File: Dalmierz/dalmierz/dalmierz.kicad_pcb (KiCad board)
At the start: 2 copper layers, 4.3 x 6.2 mm, 51 parts, among them IC1 W25Q16JVUXIQ, J1 690-005-298-486, J2 B4B-ZR_LF__SN_TF LUNA, J3 B4B-ZR_LF__SN_LCD I2C, J7 B4B-ZR_LF__SN_URM13, SW1 1-1825910-4, SW2 1-1825910-4, SW3 1-1825910-4, SW4 1-1825910-4, SW5 1-1825910-4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

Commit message: MAIN: footprinty, rozmieszczenie na PCB work in progress
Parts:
- C1, C12, C13, C14, C18, C2, C21, C22: footprint Capacitor_SMD:C_0805_2012Metric -> Capacitor_SMD:C_0603_1608Metric
- C16, C17: footprint Capacitor_SMD:C_1210_3225Metric -> Capacitor_SMD:C_0603_1608Metric
- C19, C20: footprint Capacitor_SMD:C_1206_3216Metric -> Capacitor_SMD:C_0603_1608Metric
- J2: value B4B-ZR_LF__SN_TF LUNA -> B4B-ZR TF LUNA
- J3: value B4B-ZR_LF__SN_LCD I2C -> B4B-ZR LCD
- J7: value B4B-ZR_LF__SN_URM13 -> B4B-ZR URM13
- R11: renamed from R1; footprint Resistor_SMD:R_1210_3225Metric -> Resistor_SMD:R_0603_1608Metric
- R12, R13, R14, R2, R3: footprint Resistor_SMD:R_1210_3225Metric -> Resistor_SMD:R_0603_1608Metric
- R7: footprint Resistor_SMD:R_0805_2012Metric -> Resistor_SMD:R_0603_1608Metric
- R9: footprint Resistor_SMD:R_1206_3216Metric -> Resistor_SMD:R_0603_1608Metric
- moved BT1 92.1 mm to (160.0, 108.0), turned to -90 degrees
- moved R14 89.7 mm to (140.2, 137.4)
- moved B1 84.1 mm to (118.0, 146.5), turned to 0 degrees
- moved IC1 72.3 mm to (115.7, 109.3)
- moved C19 67.7 mm to (140.9, 84.9)
- moved U5 64.6 mm to (145.2, 86.0)
- moved C12 64.5 mm to (136.1, 114.4)
- moved R9 64.2 mm to (145.2, 109.4)
- moved C14 63.7 mm to (145.2, 114.4)
- moved C13 63.5 mm to (140.2, 114.4)
- moved C7 63.1 mm to (142.2, 121.4)
- moved R12 62.9 mm to (130.2, 108.4)
- moved R13 62.9 mm to (135.2, 108.4)
- moved J2 62.3 mm to (105.5, 124.1)
- moved J3 62.3 mm to (105.5, 129.1)
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- renumbered SW7_BOOTSEL1 to SW
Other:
- outline, holes or cut-outs redrawn

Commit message: MAIN: PCB traces in progress.
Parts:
- J2: value B4B-ZR TF LUNA -> B4B-ZR_LF__SN_TF LUNA
- J3: value B4B-ZR LCD -> B4B-ZR_LF__SN_LCD I2C
- J7: value B4B-ZR URM13 -> B4B-ZR_LF__SN_URM13
- moved J7 38.8 mm to (122.9, 99.2), turned to 180 degrees
- moved C16 34.6 mm to (131.3, 108.4), turned to 180 degrees
- moved C19 34.0 mm to (131.5, 117.6)
- moved C17 33.6 mm to (135.2, 109.4), turned to 180 degrees
- moved SW7 33.0 mm to (123.8, 90.9), turned to 0 degrees
- moved D3 32.9 mm to (122.2, 116.9), turned to 0 degrees
- moved C1 32.2 mm to (146.1, 115.7)
- moved U5 31.1 mm to (131.8, 114.1), turned to 90 degrees
- moved Y1 31.0 mm to (134.8, 107.4)
- moved J3 30.9 mm to (122.9, 103.5), turned to 180 degrees
- moved R14 30.8 mm to (137.9, 106.7), turned to -90 degrees
- moved R2 29.7 mm to (129.2, 113.1), turned to -90 degrees
- moved C2 29.3 mm to (145.2, 110.9), turned to 0 degrees
- moved U4 28.5 mm to (124.1, 114.2)
- moved U2 27.7 mm to (144.4, 113.3), turned to 0 degrees
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- renumbered SW to SW7
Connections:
- R2 pad 1: Net-(U5-SCL) -> /SCL0
- R3 pad 2: Net-(U5-SDA) -> /SDA0
- U5 pad 7: Net-(U5-SDA) -> /SDA0
- U5 pad 8: Net-(U5-SCL) -> /SCL0
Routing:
- net +3V3: track 0.00 -> 128.4 mm, vias 0 -> 5
- net /BTN6: track 0.00 -> 78.2 mm, vias 0 -> 1
- net /BTN3: track 0.00 -> 72.2 mm, vias 0 -> 1
- net VBUS: track 0.00 -> 70.4 mm, vias 0 -> 1
- net /BTN5: track 0.00 -> 67.5 mm, vias 0 -> 1
- net /BTN2: track 0.00 -> 60.8 mm, vias 0 -> 1
- net /BTN4: track 0.00 -> 59.1 mm, vias 0 -> 1
- net GND: track 0.00 -> 54.0 mm
- net /BTN1: track 0.00 -> 45.8 mm, vias 0 -> 1
- net /SDA0: track 0.00 -> 34.1 mm
- net /SCL0: track 0.00 -> 28.5 mm, vias 0 -> 2
- net +1V1: track 0.00 -> 25.8 mm, vias 0 -> 2
- net /QSPI_SD3: track 0.00 -> 11.9 mm
- net /QSPI_SCLK: track 0.00 -> 10.7 mm
- net /QSPI_SS: track 0.00 -> 10.2 mm
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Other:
- outline, holes or cut-outs redrawn

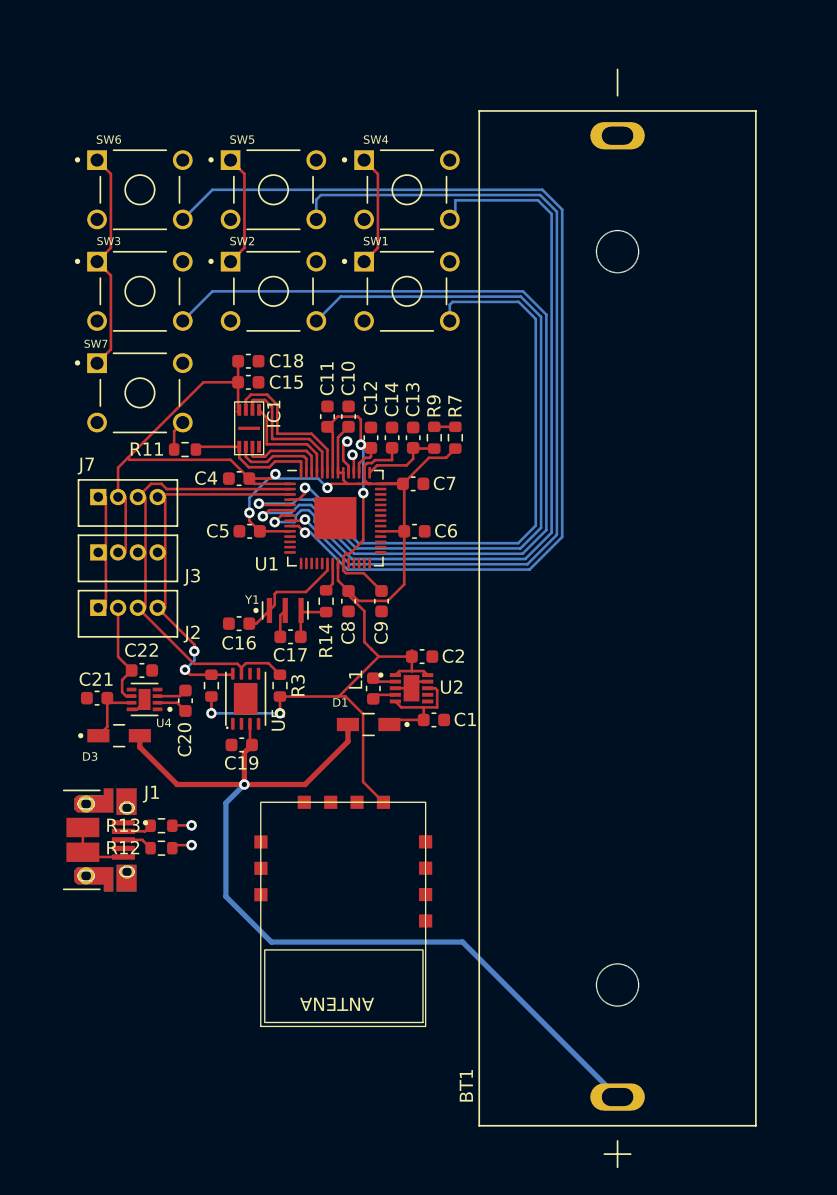
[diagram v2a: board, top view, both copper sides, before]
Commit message: MAIN: rozwiazanie problemow PCB
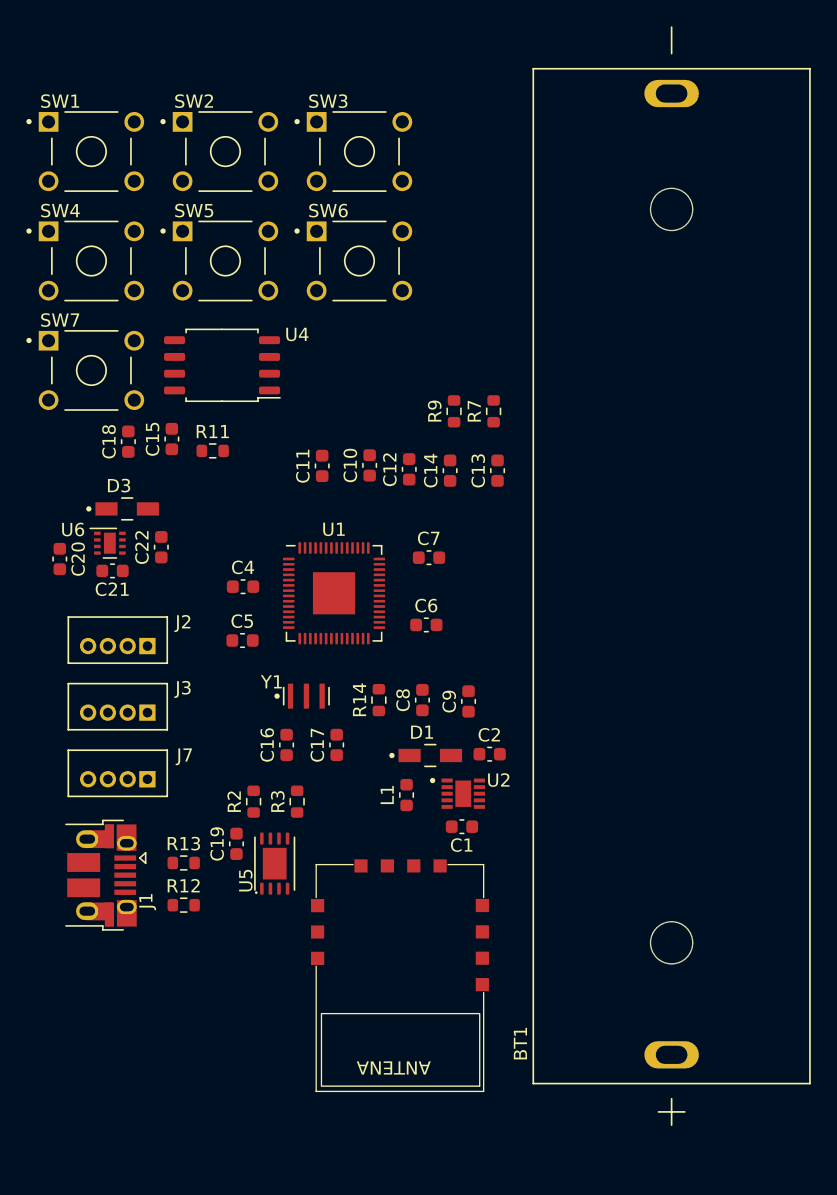
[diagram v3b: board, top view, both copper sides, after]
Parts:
- removed IC1: W25Q16JVUXIQ, W25Q16JVUXIQ:SON50P300X200X60-9N
- added U6: LM2775DSG, Package_SON:WSON-8-1EP_2x2mm_P0.5mm_EP0.9x1.6mm, F.Cu at (121.5, 102.3)
- J1: value 690-005-298-486 -> USB_B_Micro; footprint 690-005-298-486:EDAC_690-005-298-486 -> Connector_USB:USB_Micro-B_Amphenol_10103594-0001LF_Horizontal
- U4: value LM2775DSGT -> W25Q32JVSS; footprint LM2775DSGT:SON50P200X200X80-9N -> Package_SO:SOIC-8_5.23x5.23mm_P1.27mm
- moved SW1 26.2 mm to (120.1, 72.6)
- moved U4 26.0 mm to (130.0, 88.8)
- moved SW4 24.5 mm to (120.1, 80.9)
- moved J7 20.5 mm to (122.1, 119.8), turned to 0 degrees
- moved SW3 19.7 mm to (140.4, 72.6)
- moved SW6 17.5 mm to (140.4, 80.9)
- moved D3 17.2 mm to (122.8, 99.7)
- moved C20 14.4 mm to (117.7, 103.5)
- moved U5 12.7 mm to (134.0, 126.6)
- moved J3 11.3 mm to (122.1, 114.7), turned to 0 degrees
- moved SW2 11.2 mm to (130.3, 72.6)
- moved C18 11.0 mm to (122.9, 94.6), turned to 90 degrees
- moved C9 10.1 mm to (148.7, 114.3), turned to 90 degrees
- moved C16 9.88 mm to (134.9, 117.6), turned to 90 degrees
- moved C21 9.72 mm to (121.7, 104.4), turned to 180 degrees
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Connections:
- C20 pad 1: Net-(U4-C1+) -> Net-(U6-C1-)
- C20 pad 2: Net-(U4-C1-) -> Net-(U6-C1+)
- C21 pad 2: Net-(U4-VIN) -> Net-(U6-VIN)
- D3 pad 1: Net-(U4-VIN) -> Net-(U6-VIN)
- U4 pad 1: unconnected-(U4-PFM-Pad1) -> /QSPI_SS
- U4 pad 2: Net-(U4-C1-) -> /QSPI_SD1
- U4 pad 3: Net-(U4-C1+) -> /QSPI_SD2
- U4 pad 4: unconnected-(U4-OUTDIS-Pad4) -> GND
- U4 pad 5: unconnected-(U4-EN-Pad5) -> /QSPI_SD0
- U4 pad 6: +5V -> /QSPI_SCLK
- U4 pad 7: Net-(U4-VIN) -> /QSPI_SD3
- U4 pad 8: GND -> +3V3
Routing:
- net +3V3: track 128.4 -> 0.00 mm, vias 5 -> 0
- net /BTN6: track 78.2 -> 0.00 mm, vias 1 -> 0
- net /BTN3: track 72.2 -> 0.00 mm, vias 1 -> 0
- net VBUS: track 70.4 -> 0.00 mm, vias 1 -> 0
- net /BTN5: track 67.5 -> 0.00 mm, vias 1 -> 0
- net /BTN2: track 60.8 -> 0.00 mm, vias 1 -> 0
- net /BTN4: track 59.1 -> 0.00 mm, vias 1 -> 0
- net GND: track 54.0 -> 0.00 mm
- net /BTN1: track 45.8 -> 0.00 mm, vias 1 -> 0
- net /SDA0: track 34.1 -> 0.00 mm
- net /SCL0: track 28.5 -> 0.00 mm, vias 2 -> 0
- net +1V1: track 25.8 -> 0.00 mm, vias 2 -> 0
- net /QSPI_SD3: track 11.9 -> 0.00 mm
- net /QSPI_SCLK: track 10.7 -> 0.00 mm
- net /QSPI_SS: track 10.2 -> 0.00 mm
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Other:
- board outline removed

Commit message: MAIN: Koniec tworzenia PBC.
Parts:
- moved R12 36.0 mm to (131.7, 94.0)
- moved J1 34.9 mm to (127.0, 93.1)
- moved R13 34.5 mm to (131.7, 92.4)
- moved SW7 28.3 mm to (148.2, 85.2)
- moved SW4 28.3 mm to (148.2, 77.2)
- moved SW1 28.3 mm to (148.2, 69.3)
- moved C18 20.6 mm to (141.2, 85.2)
- moved R11 16.9 mm to (142.8, 85.2), turned to -90 degrees
- moved C15 16.3 mm to (139.6, 85.2)
- moved C16 13.4 mm to (143.3, 107.1), turned to 0 degrees
- moved C19 12.6 mm to (139.2, 115.5), turned to 0 degrees
- moved SW6 11.6 mm to (129.4, 77.2)
- moved SW3 11.5 mm to (129.4, 69.3)
- moved C4 10.3 mm to (137.8, 97.4)
- moved C21 10.3 mm to (131.8, 102.8)
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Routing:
- net GND: track 0.00 -> 270.1 mm
- net +3V3: track 0.00 -> 141.8 mm, vias 0 -> 6
- net /BTN3: track 0.00 -> 85.8 mm, vias 0 -> 1
- net /BTN2: track 0.00 -> 79.5 mm, vias 0 -> 1
- net VBUS: track 0.00 -> 77.6 mm, vias 0 -> 3
- net /BTN1: track 0.00 -> 73.1 mm, vias 0 -> 1
- net /BTN6: track 0.00 -> 68.2 mm, vias 0 -> 1
- net /BT_INTERRUPT: track 0.00 -> 64.6 mm, vias 0 -> 2
- net /BTN5: track 0.00 -> 62.9 mm, vias 0 -> 1
- net /BT_POWER_DOWN: track 0.00 -> 59.4 mm, vias 0 -> 2
- net /BT_LOW_POWER: track 0.00 -> 57.4 mm, vias 0 -> 2
- net /BTN4: track 0.00 -> 57.1 mm, vias 0 -> 1
- net /UART0_RX: track 0.00 -> 50.2 mm, vias 0 -> 2
- net +1V1: track 0.00 -> 49.6 mm, vias 0 -> 5
- net /UART0_TX: track 0.00 -> 49.1 mm, vias 0 -> 2
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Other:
- board outline added: 54 x 87 mm

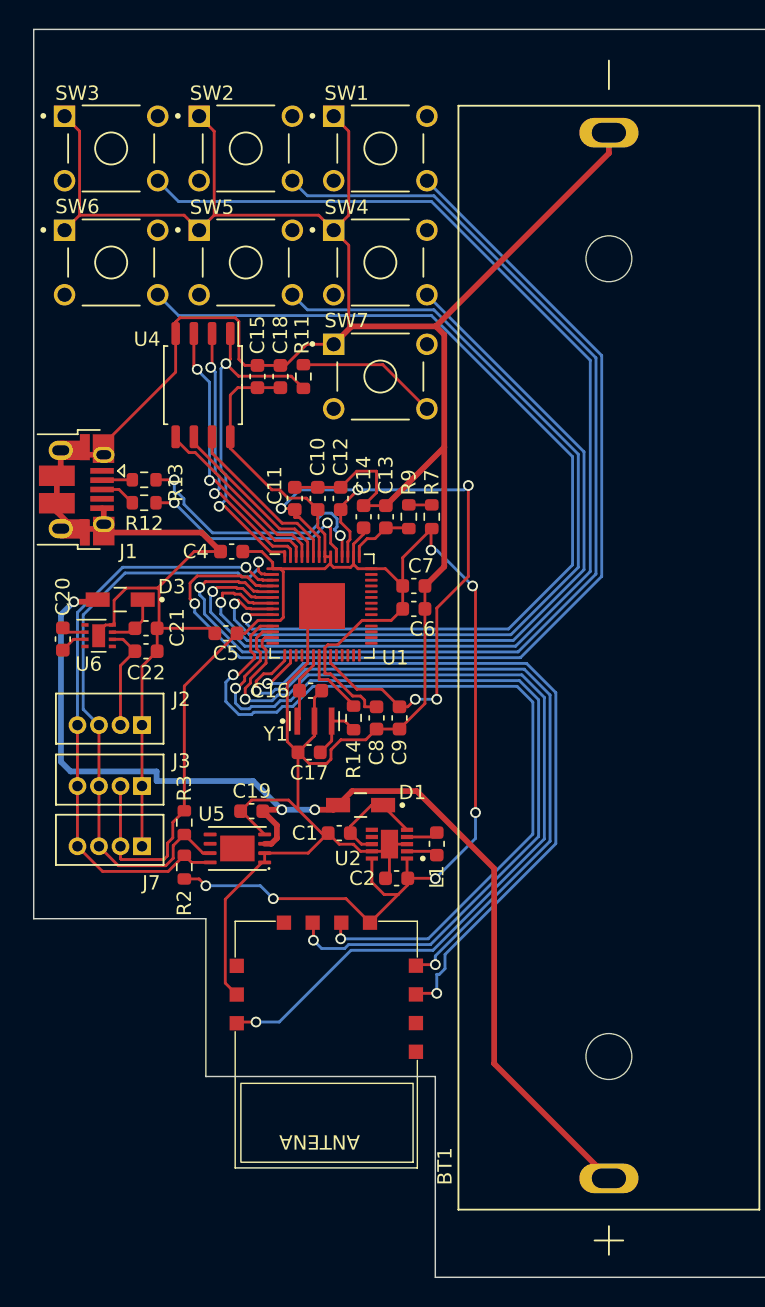
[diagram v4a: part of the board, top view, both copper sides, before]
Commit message: MAIN: Popraw błędów w PCB. Rozlanie masy itd.
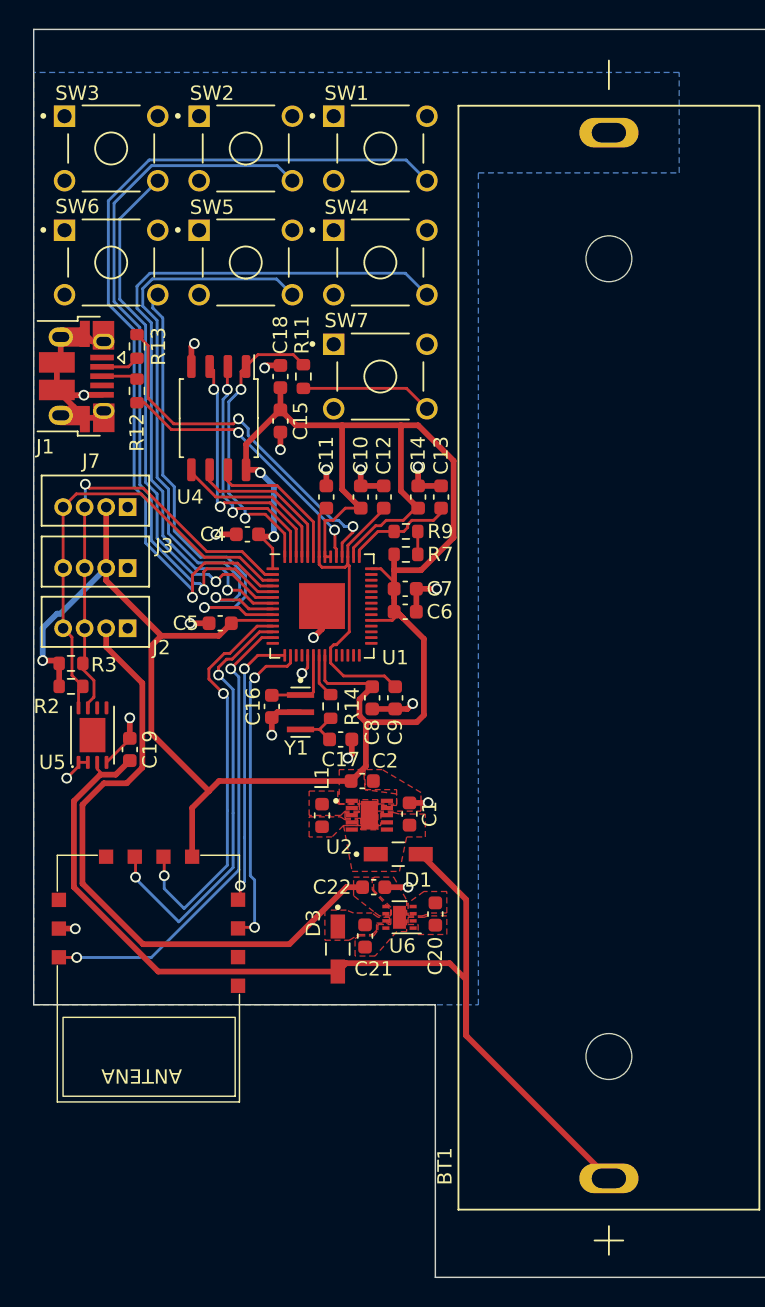
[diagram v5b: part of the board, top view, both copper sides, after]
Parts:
- moved C20 32.3 mm to (152.0, 122.7), turned to 90 degrees
- moved U6 28.7 mm to (149.5, 122.9), turned to 180 degrees
- moved D3 28.7 mm to (145.2, 125.1), turned to -90 degrees
- moved C21 26.3 mm to (147.1, 124.2), turned to 90 degrees
- moved J7 23.7 mm to (128.3, 93.8)
- moved C22 22.9 mm to (147.7, 120.8)
- moved J3 15.2 mm to (128.3, 98.1)
- moved R2 14.9 mm to (126.6, 106.8), turned to 180 degrees
- moved R3 13.6 mm to (126.6, 105.2), turned to 0 degrees
- moved B1 13.2 mm to (133.0, 132.4)
- moved U5 12.8 mm to (128.1, 110.2), turned to 90 degrees
- moved C19 9.53 mm to (130.7, 111.2), turned to -90 degrees
- moved R13 9.31 mm to (131.2, 83.1), turned to 90 degrees
- moved L1 8.24 mm to (144.1, 115.8), turned to 90 degrees
- moved J1 7.90 mm to (127.0, 85.2)
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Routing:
- net GND: track 270.1 -> 50.5 mm, vias 0 -> 20
- net /BTN3: track 85.8 -> 37.3 mm
- net +5V: track 7.49 -> 44.4 mm
- net /BTN6: track 68.2 -> 33.1 mm
- net /BT_INTERRUPT: track 64.6 -> 33.2 mm
- net /UART0_TX: track 49.1 -> 19.5 mm
- net /BT_POWER_DOWN: track 59.4 -> 30.3 mm
- net /BTN2: track 79.5 -> 50.5 mm
- net /BT_LOW_POWER: track 57.4 -> 28.4 mm
- net /UART0_RX: track 50.2 -> 22.3 mm
- net +1V1: track 49.6 -> 24.0 mm, vias 5 -> 0
- net /BTN5: track 62.9 -> 42.6 mm
- net +3V3: track 141.8 -> 158.3 mm, vias 6 -> 3
- net /SDA0: track 42.8 -> 31.8 mm
- net /BTN1: track 73.1 -> 62.2 mm
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- added copper zone on F.Cu, net +3V3
- added copper zone on F.Cu, net +5V
- added copper zone on B.Cu, net GND
- added copper zone on F.Cu, net GND
- added copper zone on F.Cu, net Net-(U2-LX1)
- added copper zone on F.Cu, net Net-(U2-LX2)
- added copper zone on F.Cu, net Net-(U2-VIN)
- added copper zone on F.Cu, net Net-(U6-C1+)
- added copper zone on F.Cu, net Net-(U6-C1-)
- added copper zone on F.Cu, net Net-(U6-VIN)
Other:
- outline, holes or cut-outs redrawn

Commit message: dalmierz koniec
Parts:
- added C3: 100n, Capacitor_SMD:C_0603_1608Metric, F.Cu at (134.3, 116.7)
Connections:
- B1 pad 10: unconnected-(B1-GND-Pad10) -> GND
- B1 pad 11: unconnected-(B1-NC-Pad11) -> GND
- B1 pad 3: unconnected-(B1-GND-Pad3) -> GND
- B1 pad 4: unconnected-(B1-GND-Pad4) -> GND
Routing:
- net GND: track 50.5 -> 57.6 mm, vias 20 -> 25

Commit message: MAIN: README dalmierz
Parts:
- moved SW3 57.5 mm to (112.2, 124.1), turned to 90 degrees
- moved SW2 52.7 mm to (112.2, 114.8), turned to 90 degrees
- moved SW1 50.9 mm to (112.2, 105.4), turned to 90 degrees
- moved SW6 47.8 mm to (120.2, 124.1), turned to 90 degrees
- moved B1 43.9 mm to (175.3, 120.5), turned to 90 degrees
- moved SW5 41.9 mm to (120.2, 114.8), turned to 90 degrees
- moved J1 41.4 mm to (128.1, 126.5), turned to 0 degrees
- moved SW4 39.7 mm to (120.2, 105.4), turned to 90 degrees
- moved R13 39.6 mm to (126.0, 122.3), turned to 180 degrees
- moved R12 36.2 mm to (129.1, 122.3), turned to 0 degrees
- moved J7 32.5 mm to (136.8, 125.2), turned to 90 degrees
- moved R2 30.6 mm to (149.7, 126.9), turned to -90 degrees
- moved R3 30.6 mm to (148.1, 126.9), turned to 90 degrees
- moved C18 30.1 mm to (128.1, 112.3), turned to 180 degrees
- moved J3 30.0 mm to (141.0, 125.2), turned to 90 degrees
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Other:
- board size 54 x 87 mm -> 87 x 54 mm
